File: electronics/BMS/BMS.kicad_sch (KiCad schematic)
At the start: 15 parts, among them J1 USB4105-GF-A, U1 BQ29700DSER, U2 BQ25180YBGR, U3 CSD16406Q3, U4 TPD2E2U06DCKR, U5 CSD16406Q3

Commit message: adjusted the pcb
Original-author: Zachariah K. Sharma <zachariah.sharma@gmail.com>
Source-commit: d12762510ca6004b4800da7825b8d34d4b880e03
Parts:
- added R5, R6: 5.1kΩ, PCM_JLCPCB:R_0402, symbol PCM_JLCPCB-Resistors:0402,5.1kΩ
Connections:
- net SHELL_GND is gone; now on net GND: J1.SH1 (SHELL_GND), J1.SH2 (SHELL_GND), J1.SH3 (SHELL_GND), J1.SH4 (SHELL_GND)
- net GND: now also U4.3 (GND), R5.1, R6.2
- net CC1: now reaches J1.A5 (CC1)
- net CC1: now also U4.1 (IO1), R5.2
- net CC2: now reaches J1.B5 (CC2)
- net CC2: now also U4.2 (IO2), R6.1
- no-connect marks 1 -> 7

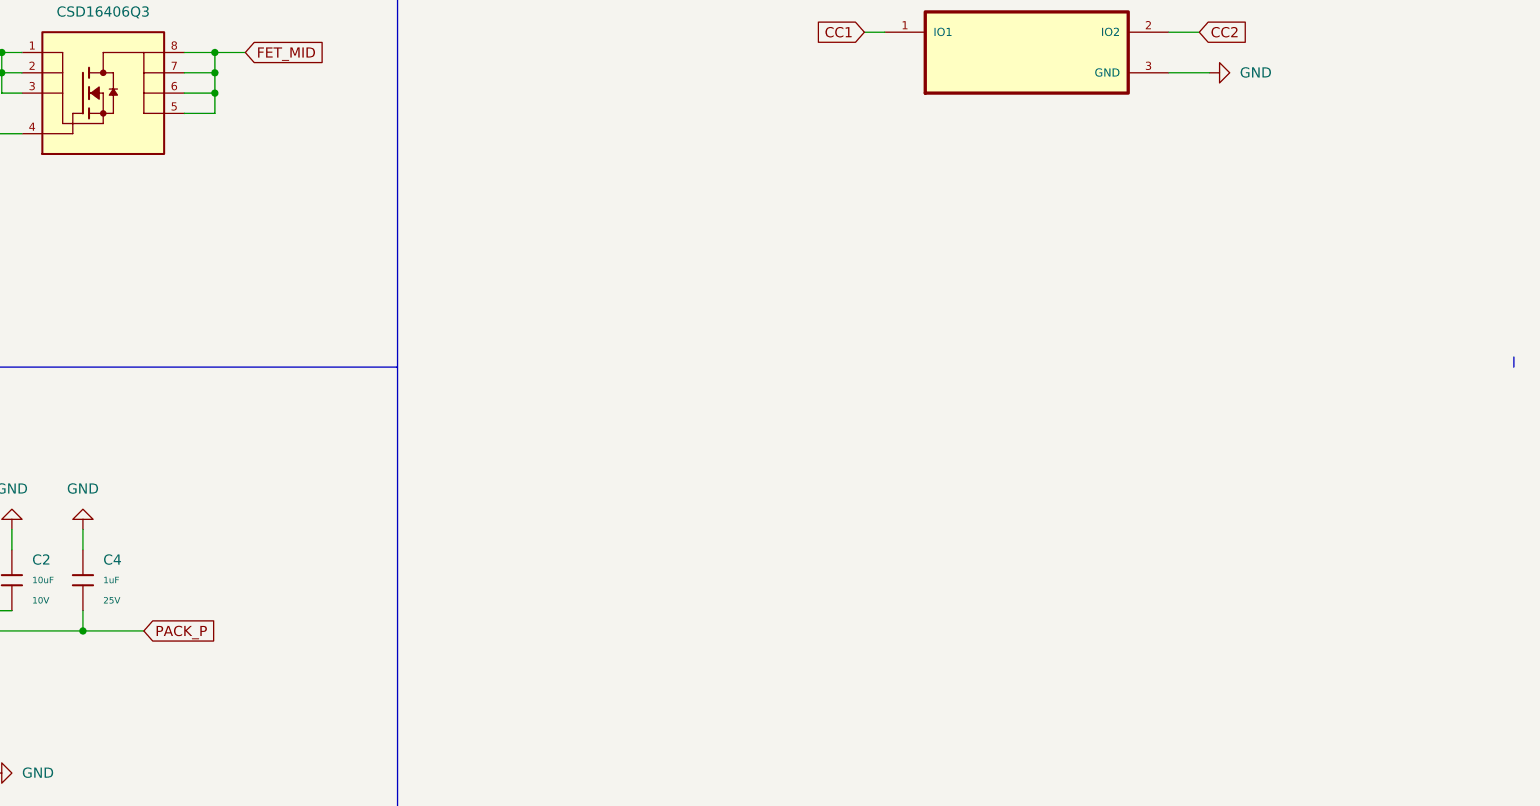
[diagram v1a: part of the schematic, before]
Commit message: Worked out the PCB Layout for the BMS, now I just need to size traces
Original-author: Zachariah K. Sharma <zachariah.sharma@gmail.com>
Source-commit: 28a479680107c7c66840ef810bf1f157462c39b5
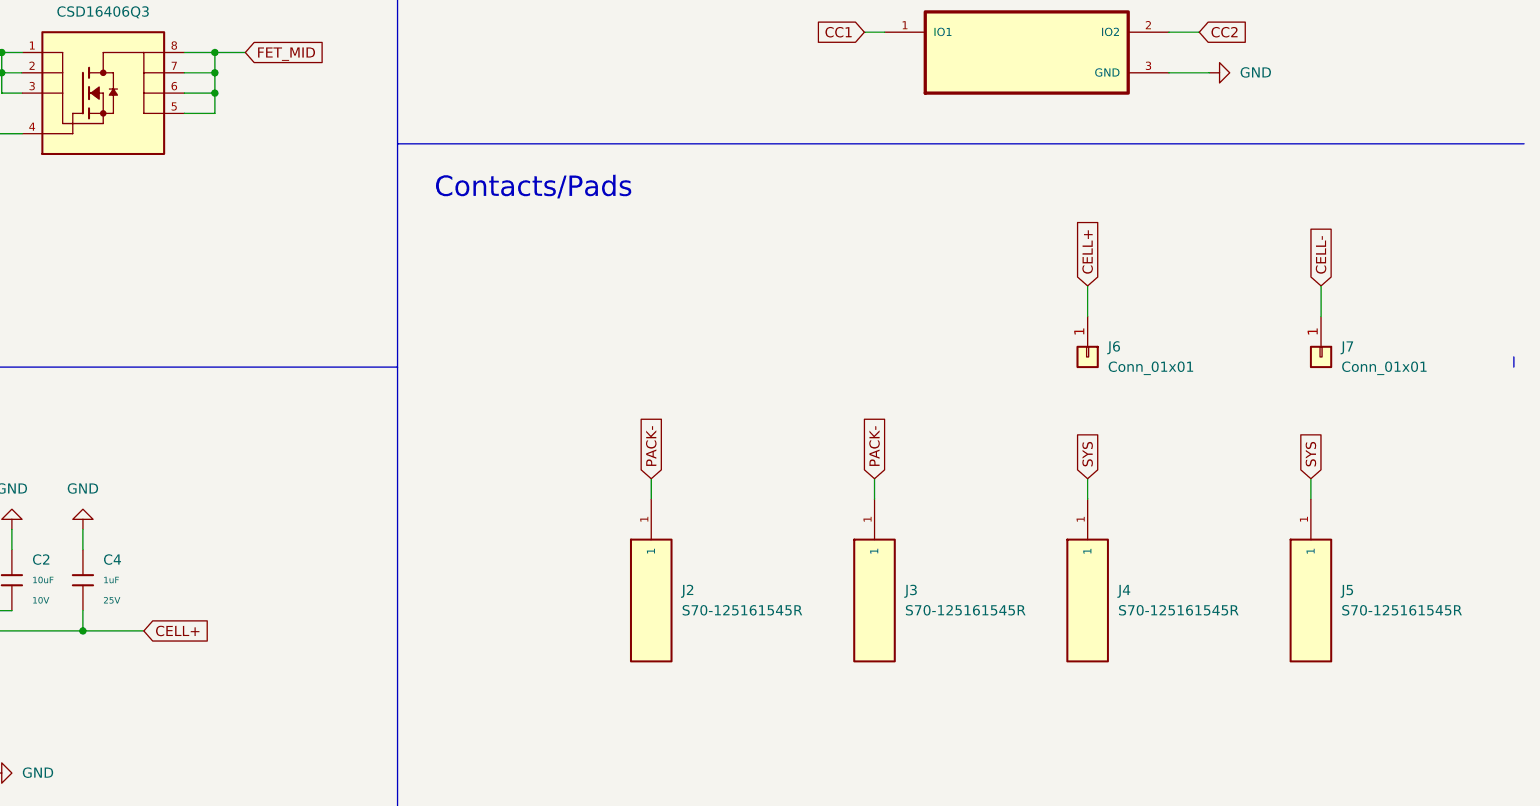
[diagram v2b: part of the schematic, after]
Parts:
- added J2, J3, J4, J5: S70-125161545R, Footprints:HARWIN_S70-125161545R, symbol S70-125161545R:S70-125161545R
- added J6, J7: Conn_01x01, MountingHole:MountingHole_2.2mm_M2_DIN965_Pad, symbol Connector_Generic:Conn_01x01
- J1: footprint USB4105-GF-A:GCT_USB4105-GF-A -> Footprints:GCT_USB4105-GF-A
- RT1: footprint NCP15XH103F03RC:THRMC1005X55N -> Footprints:THRMC1005X55N
- U1: footprint BQ29700DSER:SON50P150X150X80-6N -> Footprints:SON50P150X150X80-6N
- U2: footprint BQ25180YBGR:IC_BQ25180YBGR -> Footprints:IC_BQ25180YBGR
- U3, U5: footprint CSD16406Q3:TRANS_CSD16406Q3 -> Footprints:TRANS_CSD16406Q3
- U4: footprint TPD2E2U06DCKR:SOT65P210X110-3N -> Footprints:SOT65P210X110-3N
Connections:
- net PACK_P is gone; now on net CELL+: C4.2, U2.C2 (BAT)
- net CELL+: now also J6.1 (Pin_1)
- net CELL-: now also J7.1 (Pin_1)
- net PACK-: now also J2.1, J3.1
- net SYS: now also J4.1, J5.1
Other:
- note added: "Contacts/Pads"
- company: (none) -> Vynte
- title: (none) -> BMS

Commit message: Finalized Everything for Review, exported gerbers
Original-author: Zachariah K. Sharma <zachariah.sharma@gmail.com>
Source-commit: 3e0c8e76005ef0c547eaa410b6d8aef809166c90
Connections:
- net PACK- is gone; now on net GND: J2.1, J3.1, R2.1, U3.1, U3.2, U3.3
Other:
- company: Vynte -> (none)

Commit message: Autoprogramming, Finish off BMS, Add comps to Vent, and do a bunch of mobile stuff
Original-author: Zachariah K. Sharma <zachariah.sharma@gmail.com>
Source-commit: c8fb455aabb0719517b46fd9304eb5e5fb9f4004
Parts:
- J2, J3, J4, J5: footprint Footprints:HARWIN_S70-125161545R -> Footprints:ENIG_PAD
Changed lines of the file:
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@@
 			)
 		)
-		(property "Footprint" "Footprints:HARWIN_S70-125161545R"
+		(property "Footprint" "Footprints:ENIG_PAD"
 			(at 231.14 149.86 0)
 			(effects
@@
 			)
 		)
-		(property "Footprint" "Footprints:HARWIN_S70-125161545R"
+		(property "Footprint" "Footprints:ENIG_PAD"
 			(at 259.08 149.86 0)
 			(effects
@@
 			)
 		)
-		(property "Footprint" "Footprints:HARWIN_S70-125161545R"
+		(property "Footprint" "Footprints:ENIG_PAD"
 			(at 176.53 149.86 0)
 			(effects
@@
 			)
 		)
-		(property "Footprint" "Footprints:HARWIN_S70-125161545R"
+		(property "Footprint" "Footprints:ENIG_PAD"
 			(at 204.47 149.86 0)
 			(effects
